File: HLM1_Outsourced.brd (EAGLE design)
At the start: 51.1 x 89.4 mm, 24 parts, among them Q1 600mA/40V, Q2 IRF540

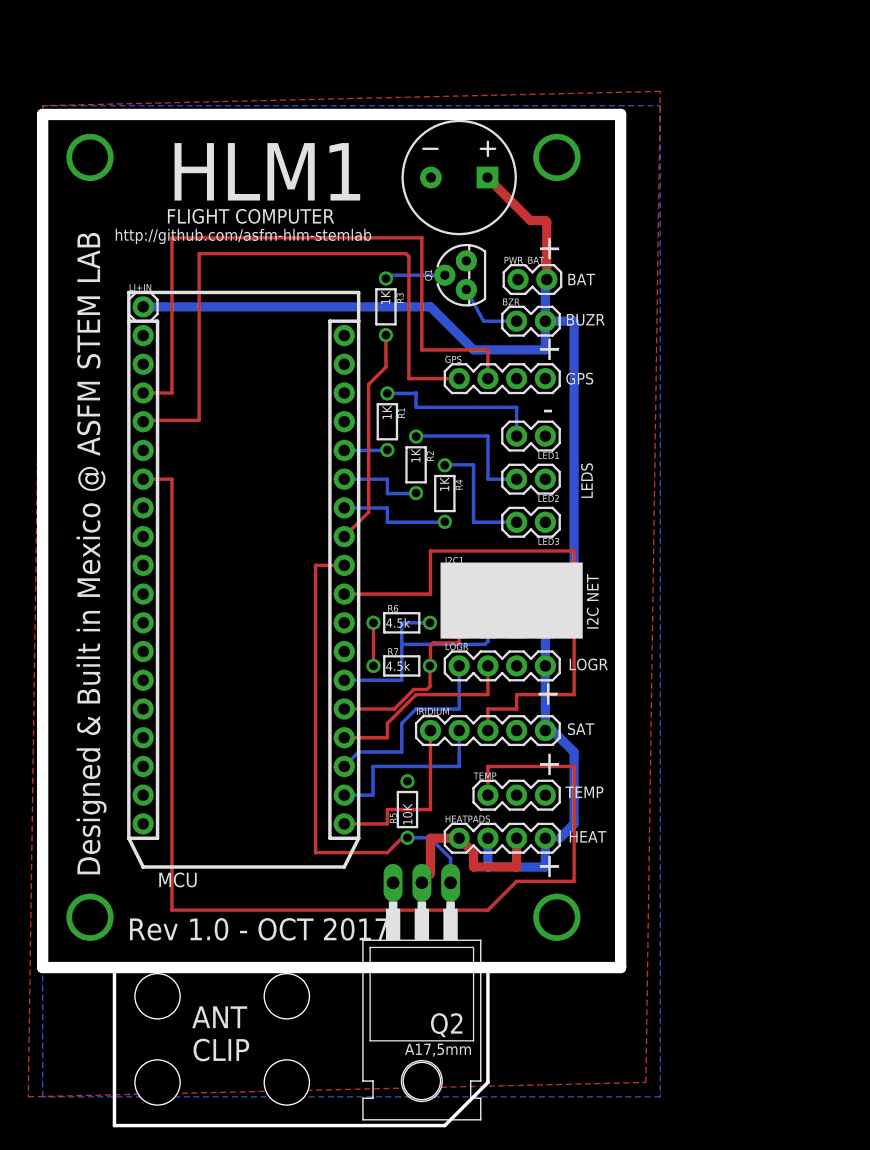
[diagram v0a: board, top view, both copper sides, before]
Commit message: Added onboard level shifter to outsourced design and other improvements
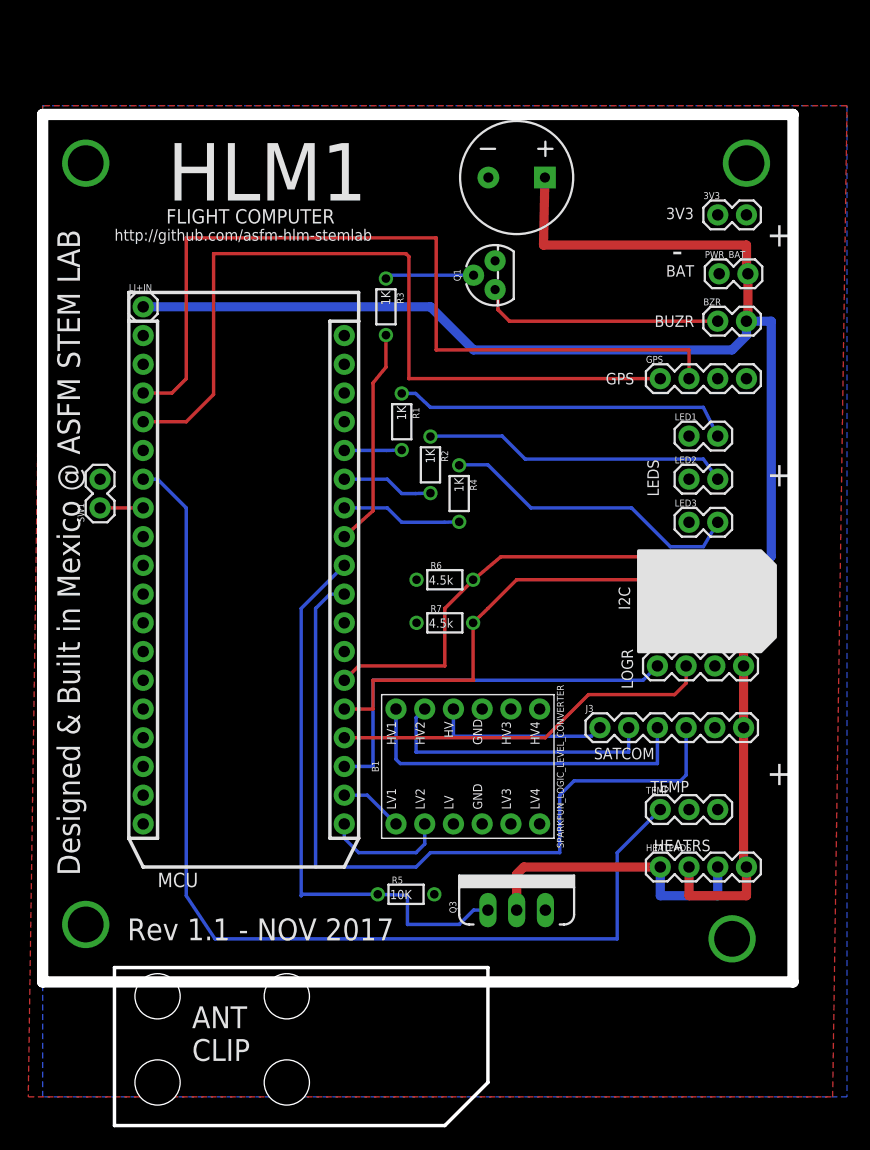
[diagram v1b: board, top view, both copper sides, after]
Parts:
- removed IRIDIUM: (no value), SparkFun-Connectors:1X05
- removed Q2: IRF540, transistor-fet:TO220
- added 3V3, SW1: (no value), SparkFun-Connectors:1X02
- added B1: SPARKFUN_LOGIC_LEVEL_CONVERTER, SparkFun-Boards:SPARKFUN_LOGIC_LEVEL_CONVERTER
- added J3: (no value), SparkFun-Connectors:1X06
- added Q3: 60V/32A/35mΩ, SparkFun-DiscreteSemi:TO220V
- moved HEATPADS 18.0 mm to (54.6, 24.1)
- moved PWR_BAT 17.8 mm to (59.8, 76.6)
- moved BZR 17.8 mm to (59.7, 72.4)
- moved GPS 17.8 mm to (54.6, 67.3)
- moved I2C1 17.5 mm to (54.4, 49.1)
- moved I2C 17.5 mm to (54.4, 45.5)
- moved LOGR 17.5 mm to (54.4, 41.9)
- moved TEMP 15.3 mm to (54.6, 29.2)
- moved LED1 12.7 mm to (57.1, 62.2), turned to 0 degrees
- moved LED2 12.7 mm to (57.1, 58.4), turned to 0 degrees
- moved LED3 12.7 mm to (57.1, 54.6), turned to 0 degrees
- moved R5 7.49 mm to (32.1, 21.7), turned to 0 degrees
- moved R6 5.39 mm to (35.6, 49.5)
- moved R7 5.39 mm to (35.6, 45.7)
- moved C1 5.08 mm to (41.9, 85.1)
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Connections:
- removed net UART5_RX: IRIDIUM.1, MCU.19
- new net 5VREF: B1.HV, J3.1
- new net N$10: B1.HV1, J3.3
- new net N$15: MCU.7, SW1.1
- new net N$6: B1.LV1, MCU.20
- new net N$7: B1.LV2, MCU.19
- net 3.3V: now also 3V3.2, B1.LV, SW1.2
- net D3: now also Q3.1; no longer Q2.1
- net GND: now also 3V3.1, B1.GND1, B1.GND2, J3.5, Q3.3; no longer IRIDIUM.4, Q2.3
- net IRWKP: now also J3.4; no longer IRIDIUM.3
- net N$11: now also Q3.2; no longer Q2.2
- net N$14: now also B1.HV2, J3.2; no longer IRIDIUM.2, MCU.20
- net V_BATT: now also J3.6; no longer IRIDIUM.5
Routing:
- net N$10: track 0.00 -> 30.9 mm
- net V_BATT: track 119.6 -> 149.9 mm
- net IRWKP: track 47.6 -> 69.2 mm
- net SCL: track 20.3 -> 40.8 mm
- net UART4_RX: track 17.6 -> 35.8 mm
- net SDA: track 26.0 -> 43.7 mm
- net N$2: track 56.6 -> 73.7 mm
- net N$12: track 53.6 -> 70.2 mm
- net UART4_TX: track 17.6 -> 33.7 mm
- net UART5_RX: track 15.9 -> 0.00 mm
- net 5VREF: track 0.00 -> 15.7 mm
- net N$19: track 11.4 -> 27.1 mm
- net N$9: track 6.10 -> 21.7 mm
- net N$8: track 15.3 -> 30.0 mm
- net N$16: track 12.7 -> 27.2 mm
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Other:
- board size 51.1 x 89.4 mm -> 66.3 x 89.4 mm
- board text added: "3V3"
- board text added: "ASFM | HLM 1 | v1.1"
- board text added: "HEATRS"
- board text added: "I2C"
- board text added: "Rev 1.1 - NOV 2017"
- board text added: "SATCOM"
- board text removed: "ASFM | HLM 1 | v1.0"
- board text removed: "HEAT"
- board text removed: "I2C NET"
- board text removed: "Rev 1.0 - OCT 2017"
- board text removed: "SAT"

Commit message: Added onboard SD CARD + Sonar Port for touchdown detection
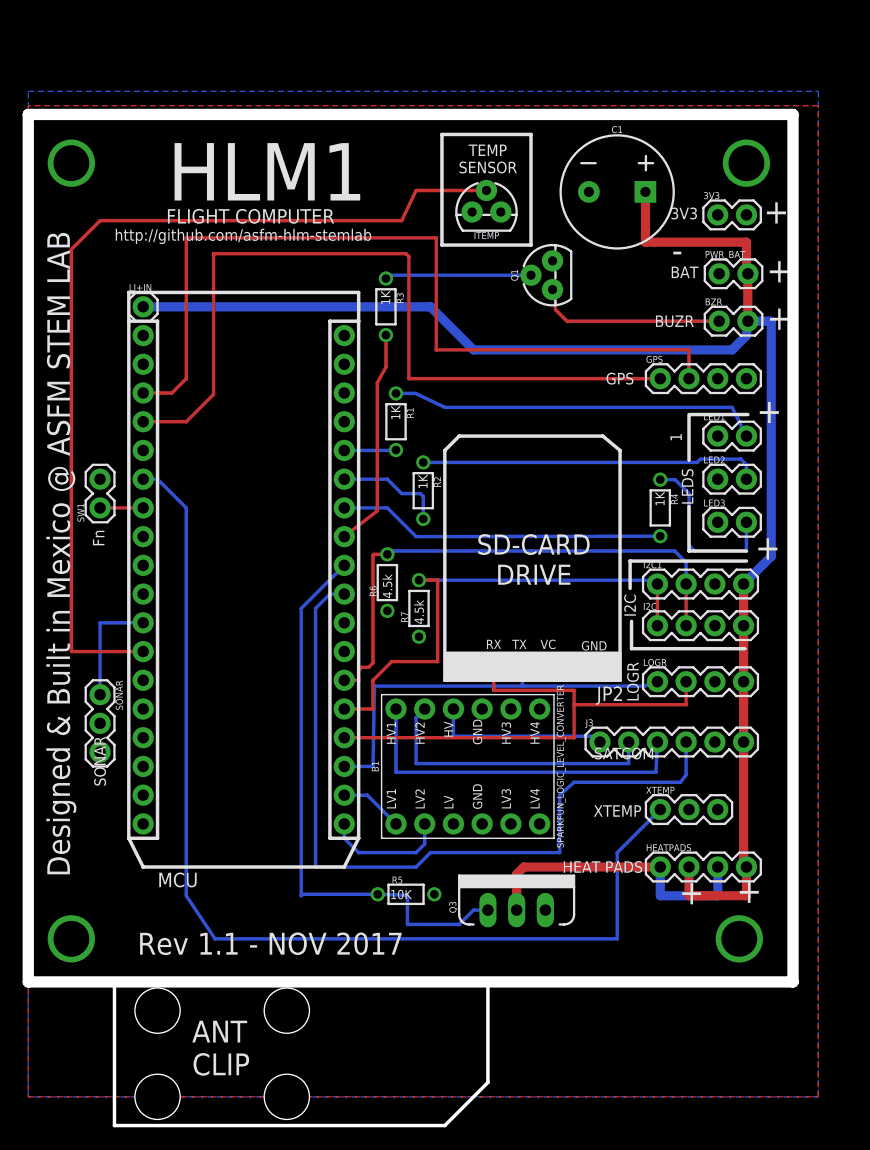
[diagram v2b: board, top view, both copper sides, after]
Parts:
- added ITEMP: (no value), SparkFun-Sensors:TO-92
- added JP2: (no value), SparkFun-Connectors:1X06_NO_SILK
- added SONAR: 455-1750-1-ND, SparkFun-Connectors:1X03
- J3: device SparkFun-Connectors:1X06 -> SparkFun-Connectors:1X06@1
- moved R4 17.8 mm to (54.6, 55.9)
- moved C1 8.98 mm to (50.8, 83.8)
- moved R6 5.09 mm to (30.5, 49.3), turned to 90 degrees
- moved Q1 5.08 mm to (45.1, 76.5)
- moved R7 2.62 mm to (33.3, 47.0), turned to 90 degrees
- moved LED1 2.54 mm to (59.7, 62.2)
- moved LED2 2.54 mm to (59.7, 58.4)
- moved LED3 2.54 mm to (59.7, 54.6)
- moved R2 2.37 mm to (33.7, 57.4)
- moved LOGR 1.40 mm to (54.4, 40.5)
- moved J3 1.27 mm to (49.3, 35.2)
- moved R1 0.51 mm to (31.2, 63.5)
- moved BZR 0.13 mm to (59.8, 72.4)
- renumbered TEMP to XTEMP
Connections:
- new net N$17: MCU.11, SONAR.1
- new net N$21: ITEMP.2, MCU.12
- net 3.3V: now also ITEMP.1, JP2.3, SONAR.3
- net GND: now also ITEMP.3, JP2.1, JP2.2, SONAR.2
- net UART4_RX: now also JP2.4
- net UART4_TX: now also JP2.5
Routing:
- net N$21: track 0.00 -> 81.3 mm
- net N$18: track 10.7 -> 29.0 mm
- net UART4_TX: track 33.7 -> 45.8 mm
- net N$19: track 27.1 -> 15.5 mm
- net V_BATT: track 149.9 -> 139.5 mm
- net N$17: track 0.00 -> 10.2 mm
- net SCL: track 40.8 -> 45.9 mm
- net N$4: track 7.87 -> 12.9 mm
- net N$9: track 21.7 -> 16.8 mm
- net SDA: track 43.7 -> 47.1 mm
- net N$16: track 27.2 -> 30.2 mm
- net N$8: track 30.0 -> 32.8 mm
- net N$13: track 8.15 -> 9.61 mm
- net IRWKP: track 69.2 -> 68.0 mm
- net N$14: track 25.1 -> 25.8 mm
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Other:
- board size 66.3 x 89.4 mm -> 67.6 x 89.4 mm
- board text added: "1"
- board text added: "Fn"
- board text added: "GND"
- board text added: "HEAT PADS"
- board text added: "RX"
- board text added: "SD-CARD DRIVE"
- board text added: "SONAR"
- board text added: "TEMP SENSOR"
- board text added: "TX"
- board text added: "VC"
- board text added: "XTEMP"
- board text removed: "HEATRS"
- board text removed: "TEMP"

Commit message: Improved design and labels
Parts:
- removed J3: (no value), SparkFun-Connectors:1X06@1
- removed JP2: (no value), SparkFun-Connectors:1X06_NO_SILK
- added SATCOM: (no value), SparkFun-Connectors:1X06@1
- added SD: (no value), SparkFun-Connectors:1X06_NO_SILK
- B1: value SPARKFUN_LOGIC_LEVEL_CONVERTER -> LOGIC LEVEL SHIFTER
- Q3: value 60V/32A/35mΩ -> MOSFET
- SONAR: value 455-1750-1-ND -> SONAR
- moved Q1 5.95 mm to (50.7, 74.4)
- moved LOGR 1.27 mm to (54.4, 39.2)
- moved XTEMP 0.76 mm to (54.6, 28.4)
- renumbered HEATPADS to HEAT
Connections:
- net 3.3V: now also SD.3; no longer JP2.3
- net 5VREF: now also SATCOM.1; no longer J3.1
- net GND: now also SATCOM.5, SD.1, SD.2; no longer J3.5, JP2.1, JP2.2
- net IRWKP: now also SATCOM.4; no longer J3.4
- net N$10: now also SATCOM.3; no longer J3.3
- net N$14: now also SATCOM.2; no longer J3.2
- net UART4_RX: now also SD.4; no longer JP2.4
- net UART4_TX: now also SD.5; no longer JP2.5
- net V_BATT: now also SATCOM.6; no longer J3.6
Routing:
- net N$9: track 16.8 -> 9.28 mm
- net N$4: track 12.9 -> 19.6 mm
- net 5VREF: track 15.5 -> 17.1 mm
- net UART4_RX: track 36.5 -> 38.0 mm
- net N$2: track 73.7 -> 72.4 mm
- net UART4_TX: track 45.8 -> 47.0 mm
- net IRWKP: track 68.0 -> 66.9 mm
- net N$14: track 25.8 -> 26.7 mm
- net N$21: track 81.3 -> 80.5 mm
- net N$10: track 31.2 -> 31.9 mm
- net N$12: track 70.2 -> 69.6 mm
- net N$1: track 92.3 -> 91.8 mm
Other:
- board text added: "BZR"
- board text removed: "BUZR"
- board text removed: "HEAT PADS"
- board text removed: "LOGR"
- board text removed: "XTEMP"

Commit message: Minor Updates
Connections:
- net N$12 renamed RX
- net N$2 renamed TX
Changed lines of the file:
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@@
 <?xml version="1.0" encoding="utf-8"?>
 <!DOCTYPE eagle SYSTEM "eagle.dtd">
-<eagle version="8.4.1">
+<eagle version="8.5.2">
 <drawing>
 <settings>
@@
 </layers>
 <board>
+<fusionsync huburn="a.cGVyc29uYWw6dWUyOWM2ZjI0" projecturn="a.cGVyc29uYWw6dWUyYWYxMDY1IzIwMTcxMTA2MTAyNjI5MDgx" f3durn="urn:adsk.wipprod:dm.lineage:U9DMslMvTZm1OZSsuvwl7A" pcbguid="3af8f604-7210-4a43-b7fa-a2a5fc980fa6" lastpulledtime="" lastsyncedchangeguid="b7256d64-2f80-e05c-89fa-ae1cbdf9443e"/>
 <plain>
 <wire x1="-1.27" y1="13.97" x2="66.345" y2="13.97" width="1" layer="20"/>
@@
 <param name="checkRestrict" value="1"/>
 <param name="checkStop" value="0"/>
+<param name="checkValues" value="0"/>
 <param name="useDiameter" value="13"/>
 <param name="maxErrors" value="50"/>
@@
 <wire x1="54.61" y1="21.59" x2="54.61" y2="24.13" width="0.8128" layer="16"/>
 </signal>
-<signal name="N$12">
+<signal name="RX">
 <contactref element="MCU" pad="4"/>
 <contactref element="GPS" pad="1"/>
@@
 <wire x1="34.885" y1="49.49" x2="33.274" y2="49.49" width="0.3048" layer="1"/>
 </signal>
-<signal name="N$2">
+<signal name="TX">
 <contactref element="MCU" pad="3"/>
 <contactref element="GPS" pad="2"/>
@@
 which will not be processed correctly with this version.
 </note>
+<note version="8.3" severity="warning">
+Since Version 8.3, EAGLE supports Fusion synchronisation.
+This feature will not be available in this version and saving
+the document will break the link to the Fusion PCB feature.
+</note>
 </compatibility>
